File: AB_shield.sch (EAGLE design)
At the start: 11 parts, among them U1 ARDUINOR3-DIMENSION, X2 MOTOR

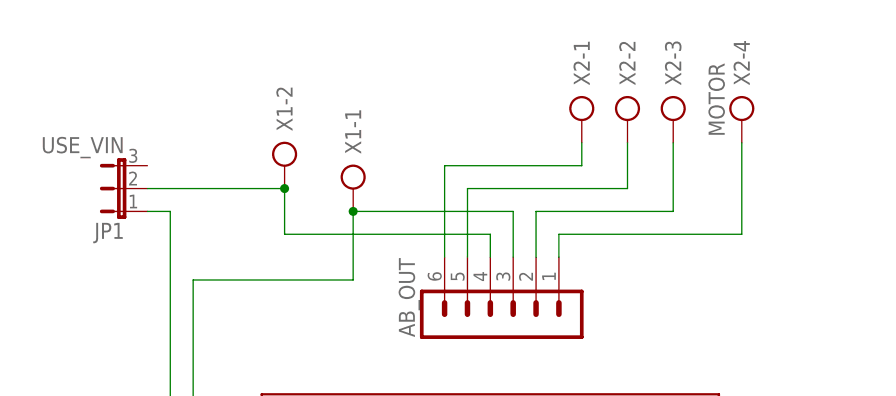
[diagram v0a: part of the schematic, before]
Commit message: Added silkscreen pinout and jumper info
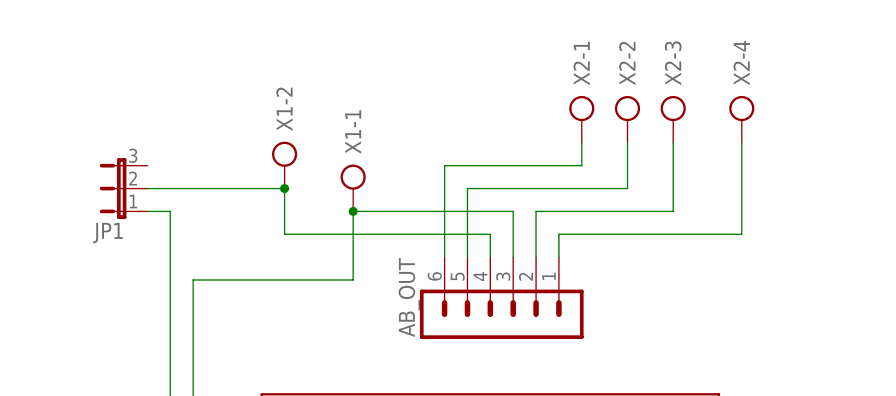
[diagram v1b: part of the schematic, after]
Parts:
- JP1: value USE_VIN -> (none)
- X2: value MOTOR -> (none)
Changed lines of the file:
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@@
 <part name="AB_OUT" library="con-lstb" deviceset="MA06-1" device=""/>
 <part name="X1" library="con-ptr500" deviceset="AK500/2-H" device=""/>
-<part name="X2" library="con-ptr500" deviceset="AK500/4" device="" value="MOTOR"/>
-<part name="JP1" library="jumper" deviceset="JP2E" device="" value="USE_VIN"/>
+<part name="X2" library="con-ptr500" deviceset="AK500/4" device=""/>
+<part name="JP1" library="jumper" deviceset="JP2E" device=""/>
 <part name="U1" library="adafruit" deviceset="ARDUINOR3" device="-DIMENSION"/>
 <part name="U$1" library="SparkFun_proto" deviceset="M17" device=""/>
